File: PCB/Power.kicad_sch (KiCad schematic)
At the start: 23 parts, among them J10 USB_C_Receptacle_USB2.0_14P, SW2 SW_Push, U1 TLV62569ADRL, U4 CP2102N-Axx-xQFN28

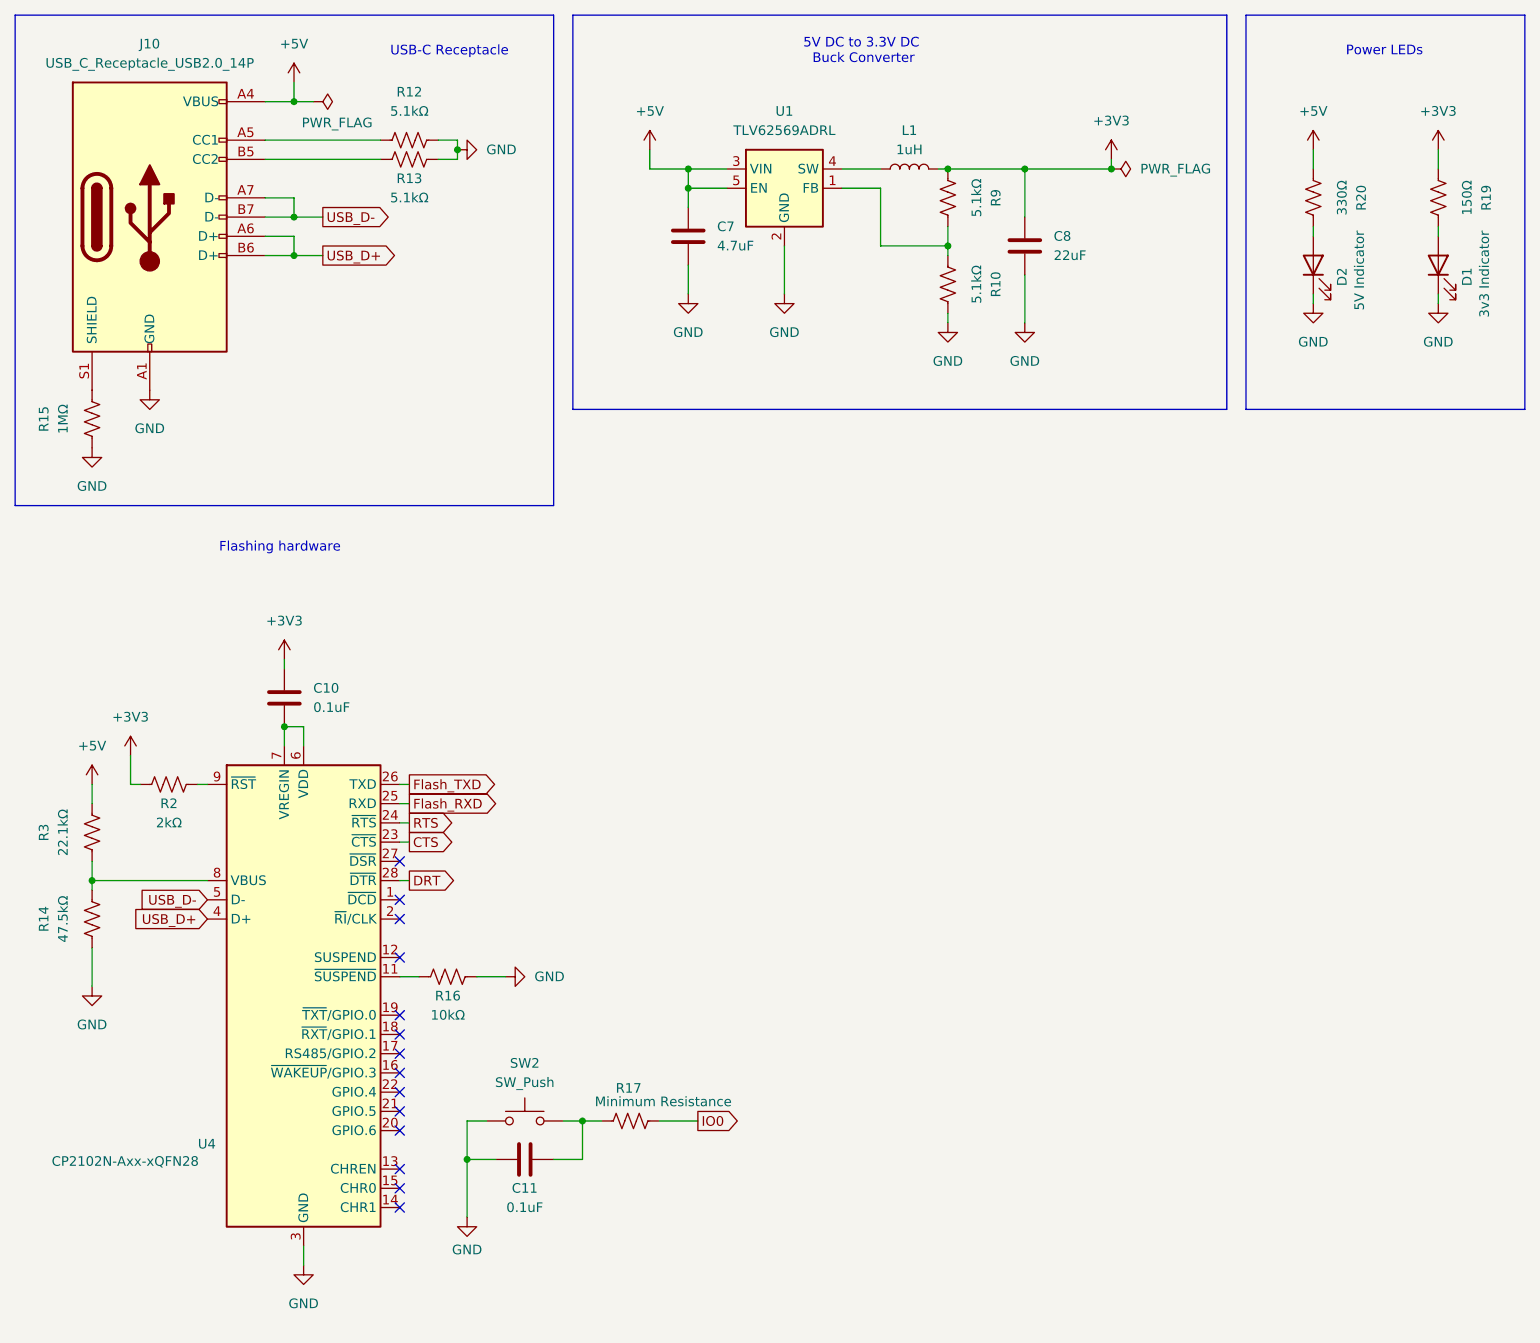
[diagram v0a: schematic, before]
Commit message: Created BOM and added USBC footprint
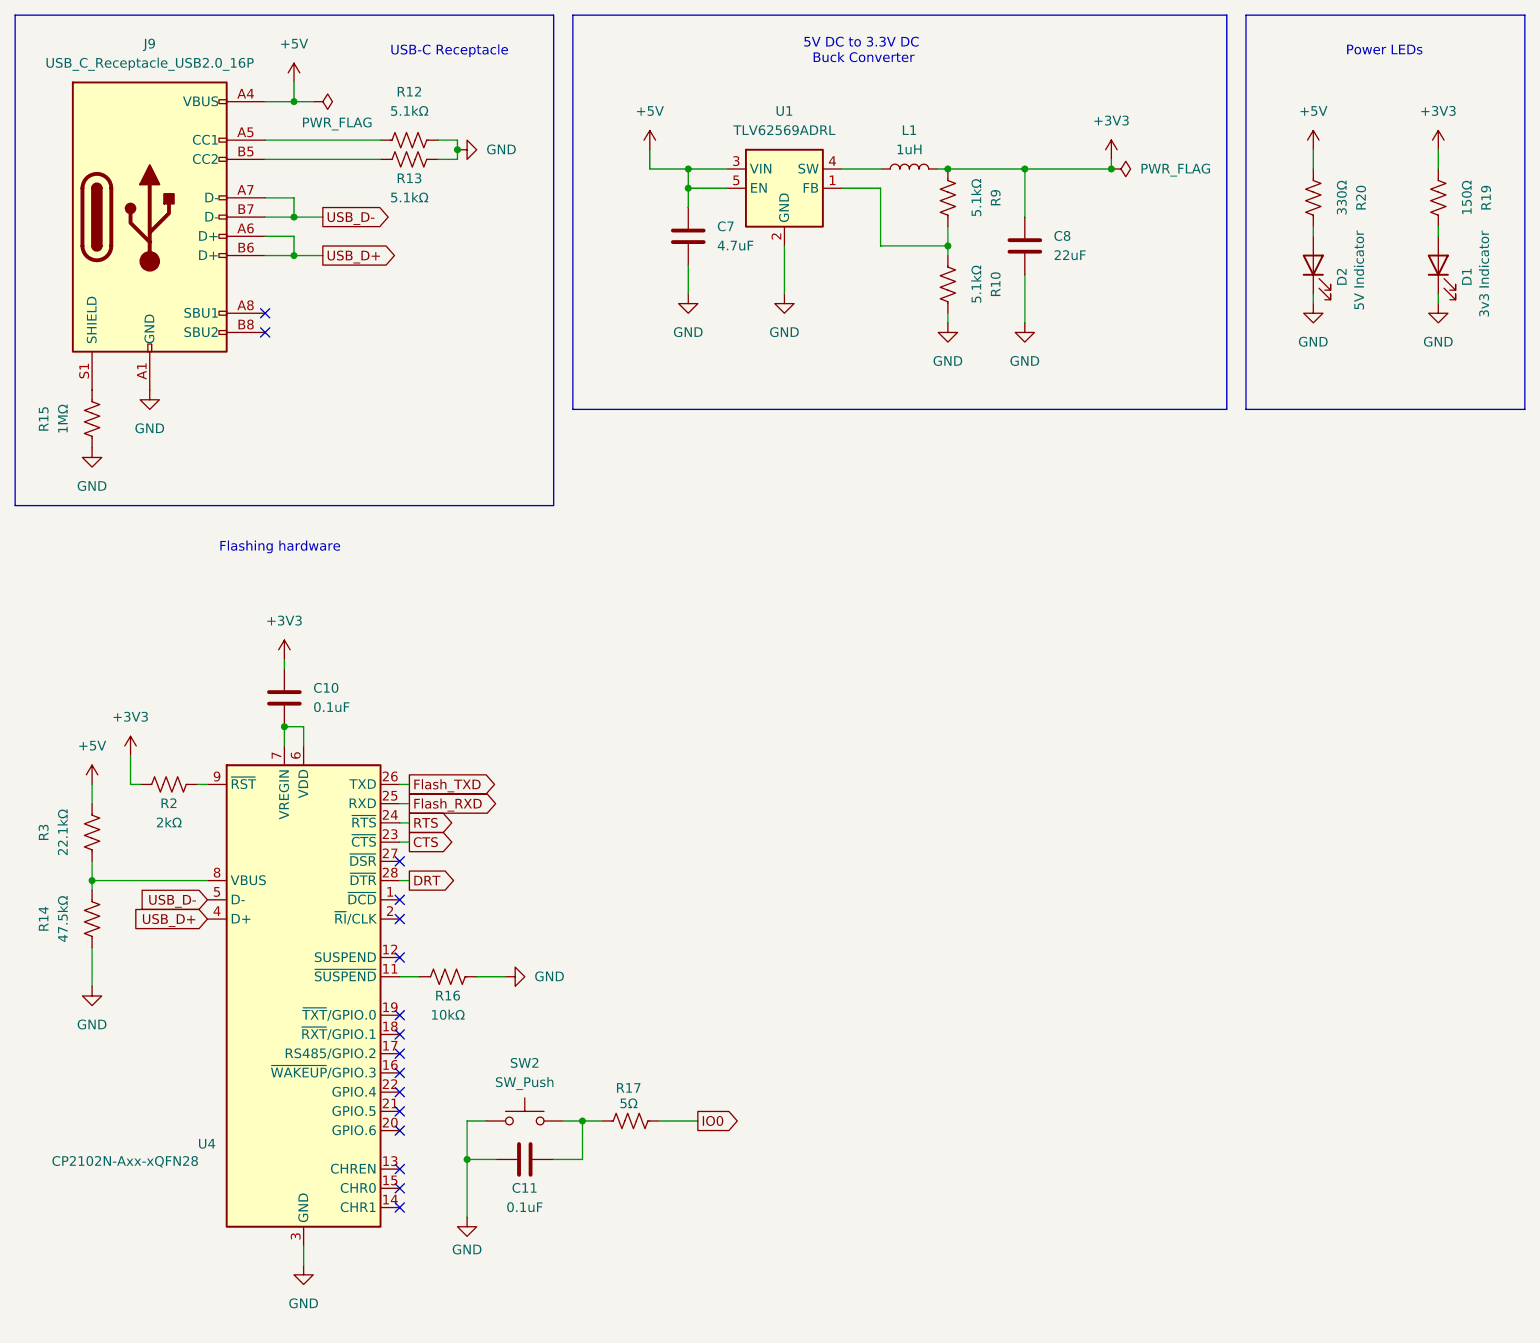
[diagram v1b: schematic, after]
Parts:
- removed J10: USB_C_Receptacle_USB2.0_14P, symbol Connector:USB_C_Receptacle_USB2.0_14P
- added J9: USB_C_Receptacle_USB2.0_16P, Connector_USB:USB_C_Receptacle_G-Switch_GT-USB-7010ASV, symbol Connector:USB_C_Receptacle_USB2.0_16P
- R17: value Minimum Resistance -> 5Ω
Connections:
- net +5V: now also J9.A4 (VBUS), J9.A9 (VBUS), J9.B4 (VBUS), J9.B9 (VBUS)
- net GND: now also J9.A1 (GND), J9.A12 (GND), J9.B1 (GND), J9.B12 (GND)
- net USB_D+: now also J9.A6 (D+), J9.B6 (D+)
- net USB_D-: now also J9.A7 (D-), J9.B7 (D-)
- net at R13.1: now also J9.B5 (CC2)
- net at R12.1: now also J9.A5 (CC1)
- net at R15.2: now also J9.S1 (SHIELD)
- no-connect marks 14 -> 16
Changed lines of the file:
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@@
 	)
 	(no_connect
+		(at 46.99 55.88)
+	)
+	(no_connect
+		(at 46.99 53.34)
+	)
+	(no_connect
 		(at 64.77 153.67)
 	)
@@
 	(wire
 		(pts
+			(xy 46.99 43.18) (xy 50.8 43.18)
+		)
+		(stroke
+			(width 0)
+			(type default)
+		)
+	)
+	(wire
+		(pts
 			(xy 88.9 165.1) (xy 88.9 160.02)
 		)
@@
 	(wire
 		(pts
+			(xy 46.99 30.48) (xy 62.23 30.48)
+		)
+		(stroke
+			(width 0)
+			(type default)
+		)
+	)
+	(wire
+		(pts
 			(xy 97.79 34.29) (xy 102.87 34.29)
 		)
@@
 	(wire
 		(pts
-			(xy 46.99 43.18) (xy 50.8 43.18)
-		)
-		(stroke
-			(width 0)
-			(type default)
-		)
-	)
-	(wire
-		(pts
 			(xy 73.66 172.72) (xy 73.66 165.1)
 		)
@@
 	(wire
 		(pts
-			(xy 46.99 40.64) (xy 50.8 40.64)
-		)
-		(stroke
-			(width 0)
-			(type default)
-		)
-	)
-	(wire
-		(pts
 			(xy 50.8 43.18) (xy 50.8 45.72)
 		)
@@
 	(wire
 		(pts
-			(xy 137.16 44.45) (xy 137.16 41.91)
+			(xy 46.99 33.02) (xy 62.23 33.02)
 		)
 		(stroke
@@
 	(wire
 		(pts
-			(xy 46.99 30.48) (xy 62.23 30.48)
+			(xy 137.16 44.45) (xy 137.16 41.91)
 		)
 		(stroke
@@
 	(wire
 		(pts
-			(xy 97.79 34.29) (xy 97.79 31.75)
+			(xy 46.99 45.72) (xy 50.8 45.72)
 		)
 		(stroke
@@
 	(wire
 		(pts
-			(xy 46.99 45.72) (xy 50.8 45.72)
+			(xy 97.79 34.29) (xy 97.79 31.75)
 		)
 		(stroke
@@
 	(wire
 		(pts
-			(xy 53.34 25.4) (xy 50.8 25.4)
+			(xy 46.99 40.64) (xy 50.8 40.64)
 		)
 		(stroke
@@
 	(wire
 		(pts
-			(xy 147.32 34.29) (xy 158.75 34.29)
+			(xy 53.34 25.4) (xy 50.8 25.4)
 		)
 		(stroke
@@
 	(wire
 		(pts
-			(xy 24.13 125.73) (xy 24.13 128.27)
+			(xy 147.32 34.29) (xy 158.75 34.29)
 		)
 		(stroke
@@
 	(wire
 		(pts
-			(xy 46.99 25.4) (xy 50.8 25.4)
+			(xy 24.13 125.73) (xy 24.13 128.27)
 		)
 		(stroke
@@
 	(wire
 		(pts
-			(xy 64.77 120.65) (xy 66.04 120.65)
+			(xy 46.99 25.4) (xy 50.8 25.4)
 		)
 		(stroke
@@
 	(wire
 		(pts
-			(xy 76.2 160.02) (xy 73.66 160.02)
+			(xy 64.77 120.65) (xy 66.04 120.65)
 		)
 		(stroke
@@
 	(wire
 		(pts
-			(xy 46.99 33.02) (xy 62.23 33.02)
+			(xy 76.2 160.02) (xy 73.66 160.02)
 		)
 		(stroke
@@
 	)
 	(symbol
+		(lib_id "Connector:USB_C_Receptacle_USB2.0_16P")
+		(at 31.75 40.64 0)
+		(unit 1)
+		(exclude_from_sim no)
+		(in_bom yes)
+		(on_board yes)
+		(dnp no)
+		(fields_autoplaced yes)
+		(property "Reference" "J9"
+			(at 31.75 17.78 0)
+			(effects
+				(font
+					(size 1.27 1.27)
+				)
+			)
+		)
+		(property "Value" "USB_C_Receptacle_USB2.0_16P"
+			(at 31.75 20.32 0)
+			(effects
+				(font
+					(size 1.27 1.27)
+				)
+			)
+		)
+		(property "Footprint" "Connector_USB:USB_C_Receptacle_G-Switch_GT-USB-7010ASV"
+			(at 35.56 40.64 0)
+			(effects
+				(font
+					(size 1.27 1.27)
+				)
+				(hide yes)
+			)
+		)
+		(property "Datasheet" "https://www.usb.org/sites/default/files/documents/usb_type-c.zip"
+			(at 35.56 40.64 0)
+			(effects
+				(font
+					(size 1.27 1.27)
+				)
+				(hide yes)
+			)
+		)
+		(property "Description" "USB 2.0-only 16P Type-C Receptacle connector"
+			(at 31.75 40.64 0)
+			(effects
+				(font
+					(size 1.27 1.27)
+				)
+				(hide yes)
+			)
+		)
+		(pin "A1"
+		)
+		(pin "A12"
+		)
+		(pin "S1"
+		)
+		(pin "A9"
+		)
+		(pin "B12"
+		)
+		(pin "B5"
+		)
+		(pin "B6"
+		)
+		(pin "A4"
+		)
+		(pin "A5"
+		)
+		(pin "A8"
+		)
+		(pin "B8"
+		)
+		(pin "B1"
+		)
+		(pin "B7"
+		)
+		(pin "B9"
+		)
+		(pin "A7"
+		)
+		(pin "A6"
+		)
+		(pin "B4"
+		)
+		(instances
+			(project ""
+				(path "/38abc652-c887-4ef7-a45f-d93ca7f4b2d6/2d9f036a-c70f-4011-9e39-88b7ded8327f"
+					(reference "J9")
+					(unit 1)
+				)
+			)
+		)
+	)
+	(symbol
 		(lib_id "power:GND")
 		(at 147.32 54.61 0)
@@
 			)
 		)
-		(property "Value" "Minimum Resistance"
-			(at 99.568 157.48 90)
+		(property "Value" "5Ω"
+			(at 94.996 157.734 90)
 			(effects
 				(font
@@
 					(unit 1)
 				)
-			)
-		)
-	)
-	(symbol
-		(lib_id "Connector:USB_C_Receptacle_USB2.0_14P")
-		(at 31.75 40.64 0)
-		(unit 1)
-		(exclude_from_sim no)
-		(in_bom yes)
-		(on_board yes)
-		(dnp no)
-		(fields_autoplaced yes)
-		(property "Reference" "J10"
-			(at 31.75 17.78 0)
-			(effects
-				(font
-					(size 1.27 1.27)
-				)
-			)
-		)
-		(property "Value" "USB_C_Receptacle_USB2.0_14P"
-			(at 31.75 20.32 0)
-			(effects
-				(font
-					(size 1.27 1.27)
-				)
-			)
-		)
-		(property "Footprint" ""
-			(at 35.56 40.64 0)
-			(effects
-				(font
-					(size 1.27 1.27)
-				)
-				(hide yes)
-			)
-		)
-		(property "Datasheet" "https://www.usb.org/sites/default/files/documents/usb_type-c.zip"
-			(at 35.56 40.64 0)
-			(effects
-				(font
-					(size 1.27 1.27)
-				)
-				(hide yes)
-			)
-		)
-		(property "Description" "USB 2.0-only 14P Type-C Receptacle connector"
-			(at 31.75 40.64 0)
-			(effects
-				(font
-					(size 1.27 1.27)
-				)
-				(hide yes)
-			)
-		)
-		(pin "B12"
-		)
-		(pin "A1"
-		)
-		(pin "A6"
-		)
-		(pin "B4"
-		)
-		(pin "B1"
-		)
-		(pin "A9"
-		)
-		(pin "A4"
-		)
-		(pin "A7"
-		)
-		(pin "A5"
-		)
-		(pin "B6"
-		)
-		(pin "B9"
-		)
-		(pin "S1"
-		)
-		(pin "A12"
-		)
-		(pin "B5"
-		)
-		(pin "B7"
-		)
-		(instances
-			(project ""
-				(path "/38abc652-c887-4ef7-a45f-d93ca7f4b2d6/2d9f036a-c70f-4011-9e39-88b7ded8327f"
-					(reference "J10")
-					(unit 1)
-				)

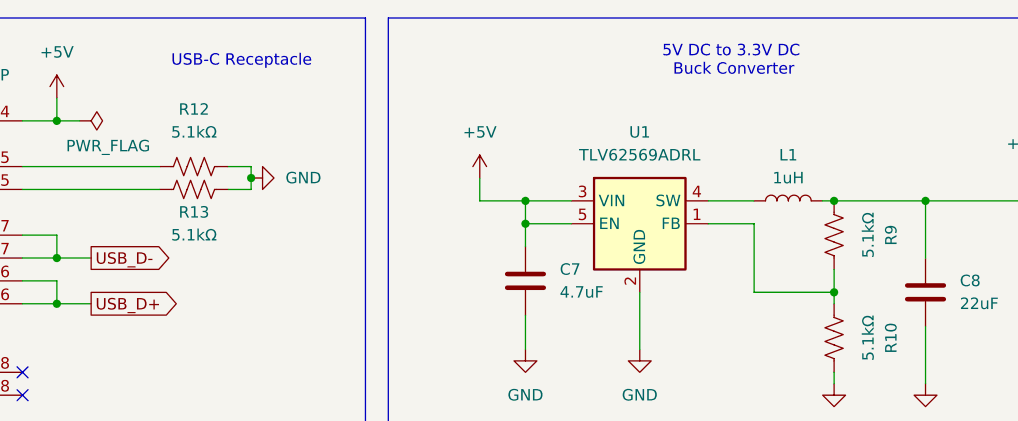
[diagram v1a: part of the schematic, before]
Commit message: Some updates suggested by Ryan (The 1 sem senior design prof)
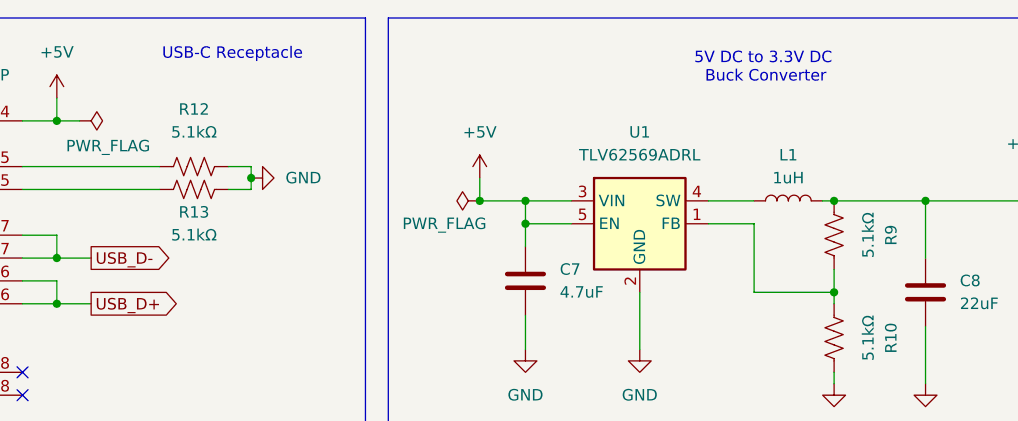
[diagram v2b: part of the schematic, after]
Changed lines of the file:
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@@
 	(text "5V DC to 3.3V DC\n Buck Converter"
 		(exclude_from_sim no)
-		(at 125.73 18.796 0)
+		(at 129.286 19.558 0)
 		(effects
 			(font
@@
 	(text "USB-C Receptacle \n"
 		(exclude_from_sim no)
-		(at 63.5 19.558 0)
+		(at 62.484 18.796 0)
 		(effects
 			(font
@@
 	(junction
 		(at 147.32 34.29)
+		(diameter 0)
+		(color 0 0 0 0)
+	)
+	(junction
+		(at 97.79 34.29)
 		(diameter 0)
 		(color 0 0 0 0)
@@
 					(unit 1)
 				)
+			)
+		)
+	)
+	(symbol
+		(lib_id "power:PWR_FLAG")
+		(at 97.79 34.29 90)
+		(unit 1)
+		(exclude_from_sim no)
+		(in_bom yes)
+		(on_board yes)
+		(dnp no)
+		(property "Reference" "#FLG03"
+			(at 95.885 34.29 0)
+			(effects
+				(font
+					(size 1.27 1.27)
+				)
+				(hide yes)
+			)
+		)
+		(property "Value" "PWR_FLAG"
+			(at 98.552 36.83 90)
+			(effects
+				(font
+					(size 1.27 1.27)
+				)
+				(justify left)
+			)
+		)
+		(property "Footprint" ""
+			(at 97.79 34.29 0)
+			(effects
+				(font
+					(size 1.27 1.27)
+				)
+				(hide yes)
+			)
+		)
+		(property "Datasheet" "~"
+			(at 97.79 34.29 0)
+			(effects
+				(font
+					(size 1.27 1.27)
+				)
+				(hide yes)
+			)
+		)
+		(property "Description" "Special symbol for telling ERC where power comes from"
+			(at 97.79 34.29 0)
+			(effects
+				(font
+					(size 1.27 1.27)
+				)
+				(hide yes)
+			)
+		)
+		(pin "1"
+		)
+		(instances
+			(project "Smart_Backpack"
+				(path "/38abc652-c887-4ef7-a45f-d93ca7f4b2d6/2d9f036a-c70f-4011-9e39-88b7ded8327f"
+					(reference "#FLG03")
+					(unit 1)
+				)

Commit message: Alert: Fat inductor incoming
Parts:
- L1: footprint Inductor_SMD:L_1206_3216Metric_Pad1.42x1.75mm_HandSolder -> WeBench_Inductor:IND_BOURNS_SRN8040
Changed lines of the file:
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@@
 			)
 		)
-		(property "Footprint" "Inductor_SMD:L_1206_3216Metric_Pad1.42x1.75mm_HandSolder"
+		(property "Footprint" "WeBench_Inductor:IND_BOURNS_SRN8040"
 			(at 132.08 34.29 0)
 			(effects
